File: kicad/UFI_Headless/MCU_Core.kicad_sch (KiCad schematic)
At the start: 85 parts, among them J12 FRONT, J20 GUARD, J21 LA, J4 SWD, J5 DBG_UART, SW1 RESET, SW2 BOOT, U11 APS6404L-3SQR-SN, U15 CSNP32GCR01-AOW, U5 STM32H723ZGT6, Y1 25MHz CL=12pF

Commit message: KiCad v0.7 rework, stage A9c (owner decisions of 2026-10-24): TCXO, RTC and humidity sensor on MCU_Core - X1 25 MHz TCXO HCI TC32H4-25.000-33GNDTNL (C5119013, HCMOS, +-2.5 ppm, JLC stock 1270; alternative ECS-TXO-3225-250-TR C2451321, both 1 E/D-or-NC, 2 GND, 3 OUT, 4 VDD per datasheet drawings) replaces the crystal Y1 with C38/C39: OUT drives HSE_IN (PH0), PH1 gets a no-connect, pin 1 goes to +3V3 through R132 10k, C75 100 nF at VDD, footprint Oscillator_SMD_Abracon_ASE-4Pin_3.2x2.5mm (pad order checked against both drawings); RTC: Y3 32.768 kHz Epson FC-135 Q13FC13500002 (C48615, CL 7 pF, ESR 70k; alternative Abracon ABS07 C276424) on PC14/PC15 (the two no-connects are gone) with C76/C77 10 pF C0G (C1634; CL = 5 pF + ~2 pF stray), gm_crit = 4*ESR*(2*pi*f)^2*(C0+CL)^2 = 0.76 uA/V so the LSE drive is medium-high; VBAT (pin 6) separated from +3V3 (wire and #PWR088 removed): BT1 CR2032 holder MYOUNG BS-07-A1BJ001 (C2979167, THT, KiCad footprint pad 1 = + verified against the holder drawing: + leg 12.4 mm from the cell centre) + C78 100 nF + PWR_FLAG; U25 SHT40-AD1B-R2 (C2909890, JLC stock 19423, I2C 0x44) + C79 100 nF on I2C_SCL/I2C_SDA next to the pads TP10-TP13, footprint without the die pad (Sensirion: do not solder it). Notes on the sheet for all three blocks. Four library symbols (ASE-xxxMHz, Crystal, Battery_Cell, SHT4x) were copied into the sheet cache by script because the KiCad MCP cannot inject into MCU_Core (its naive parenthesis counter trips over the STM32 pin names) - sub-unit names stay unqualified as KiCad writes them. ERC over the whole project 0 errors / 0 warnings (build/erc.rpt). Firmware in the same commit: ufi_clock.c tries RCC_HSE_BYPASS first (v1.0 TCXO) and falls back through RCC_HSE_OFF to RCC_HSE_ON after the 100 ms HSE timeout (v0.x crystal; RCC_HSE_ON alone would leave HSEBYP set), ufi_clock_hse_bypass() reports the result; new ufi_clock_rtc_init() (backup access, RTCAPB clock, backup-domain reset only for a stale non-LSE RTCSEL, LSE mediu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
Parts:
- removed C38, C39: 18pF C0G, Capacitor_SMD:C_0603_1608Metric, symbol Device:C
- removed Y1: 25MHz CL=12pF, Crystal:Crystal_SMD_3225-4Pin_3.2x2.5mm, symbol Device:Crystal_GND24
- added BT1: CR2032, Battery:BatteryHolder_MYOUNG_BS-07-A1BJ001_CR2032, symbol Device:Battery_Cell
- added C75, C78, C79: 100nF, Capacitor_SMD:C_0603_1608Metric, symbol Device:C
- added C76, C77: 10pF C0G, Capacitor_SMD:C_0603_1608Metric, symbol Device:C
- added R132: 10k, Resistor_SMD:R_0603_1608Metric, symbol Device:R
- added U25: SHT40-AD1B, Sensor_Humidity:Sensirion_DFN-4_1.5x1.5mm_P0.8mm_SHT4x_NoCentralPad, symbol Sensor_Humidity:SHT4x
- added X1: 25MHz TCXO HCMOS, Oscillator:Oscillator_SMD_Abracon_ASE-4Pin_3.2x2.5mm, symbol Oscillator:ASE-xxxMHz
- added Y3: 32.768kHz CL=7pF, Crystal:Crystal_SMD_3215-2Pin_3.2x1.5mm, symbol Device:Crystal
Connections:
- net +3V3: now also C75.1, C79.1, R132.1, U25.3 (VDD), X1.4 (Vdd); no longer U5.6 (VBAT)
- net GND: now also BT1.2 (-), C75.2, C76.2, C77.2, C78.2, C79.2, U25.4 (VSS), X1.2 (GND)
- net HSE_IN: now also X1.3 (OUT)
- net I2C_SCL: now also U25.2 (SCL)
- net I2C_SDA: now also U25.1 (SDA)
- net OSC32_IN: now reaches U5.8 (PC14)
- net OSC32_IN: now also C76.1, Y3.1
- net OSC32_OUT: now reaches U5.9 (PC15)
- net OSC32_OUT: now also C77.1, Y3.2
- net HSE_OUT: no longer names the net of U5.24 (PH1)
- new net VBAT: BT1.1 (+), C78.1, U5.6 (VBAT)
- new net X1_EN: R132.2, X1.1 (EN)
- no-connect marks 24 -> 23
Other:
- note added: "A9c (24.10.2026): X1 25 MHz TCXO (HCI TC32H4, HCMOS, +-2.5 ppm) replaces Y1/C38/C39 - OUT to OSC_IN (PH0), PH1 open, HSE runs in bypass; pin 1 E/D or NC tied to +3V3 via R132 (both HCI and the ECS alternative use 1 EN/NC, 2 GND, 3 OUT, 4 VDD). RTC: Y3 32.768 kHz Epson FC-135 (CL 7 pF, ESR 70k max) on PC14/PC15 with C76/C77 10 pF (CL = 10/2 + ~2 pF stray), gm_crit = 4*ESR*(2*pi*f)^2*(C0+CL)^2 = 0.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"
- note added: "A9c: U25 SHT40-AD1B humidity/temperature sensor (I2C 0x44, C2909890) on the I2C1 pads TP10-TP13 with C79 100 nF; pull-ups R19/R20 already on the bus. DFN-4 die pad not soldered (Sensirion recommendation). Layout (B3): at the air-inlet edge, away from U4/U19 and the drive supply path. Firmware reads it from stage A10 on."

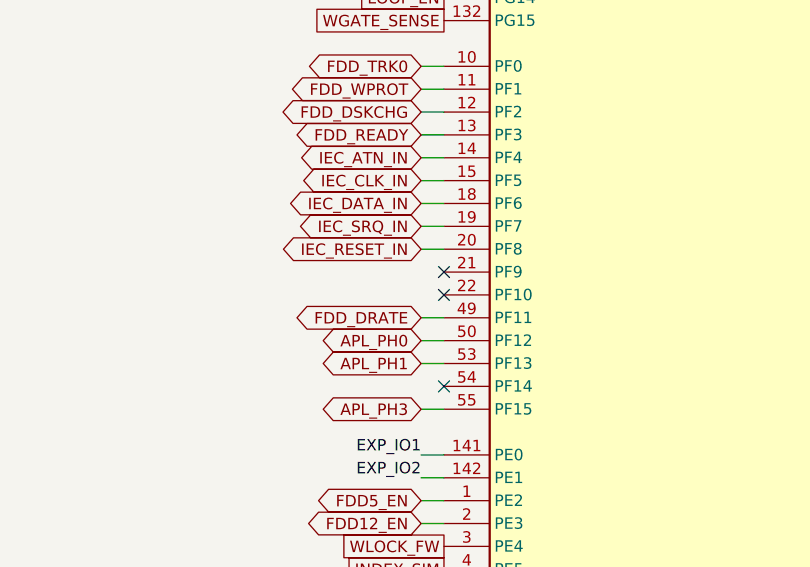
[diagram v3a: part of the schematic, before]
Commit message: KiCad v0.7 rework, stage A11c (owner's device-comparison list M2, order decided 2026-10-24: supply first): drive supplies through two TPS25921A eFuses - Power sheet: U28 (5 V) and U29 (12 V) TI TPS25921ADR (C189199, SOIC-8, JLC stock 681; new project symbol UFI_Headless:TPS25921A with the datasheet pinout 1 GND, 2 SS, 3 ENUV, 4 IN, 5 OUT, 6 FLT, 7 ILIM, 8 OVP) replace the polyfuses F2/F3 and the AO3401A/2N7002 switches Q1-Q4 with their gate network R27/R30/R32; R136/R142 150k (C22807) set the current limit to 1.43-1.7 A (datasheet table for R_ILIM = 150 k), OVP dividers R133/R134 33k/10k = 6.0 V and R138/R139/R140 100k/(10k+1k) = 14.0 V against the 1.39 V threshold (basic parts only, 91k/11k are extended), ENUV from FDD5_EN/FDD12_EN through R135/R141 10k while the existing 100k pull-downs R28/R31 keep both rails off in reset (ENUV threshold 1.39 V, 3.0 V applied), C81 2.2 nF (C1604) and C83 1 nF (C1588) give about 2.5 ms output ramp (datasheet: 1.2 nF = 3 ms at 11 V; measure at bring-up), C80/C82 100 nF at IN, FLT open drain with R137/R143 10k to +3V3 on the new global nets FLT5/FLT12; the shunts R26/R29 with U12/U13 INA180 stay behind the eFuse outputs (FDD5_F/FDD12_F -> shunt -> FDD_5V/FDD_12V, the old FDD5_S/FDD12_S nets are gone); D3 SMAJ15CA -> SMAJ13A (Diodes SMAJ13A-13-F C110519). MCU_Core: PF9 = FLT5, PF10 = FLT12 (no-connects removed). Old v0.2/v0.5 notes replaced by an A11c note. ERC over the whole project 0 errors / 0 warnings (build/erc.rpt). Firmware in the same commit: board.h/board_headless.c PIN_FLT5/PIN_FLT12 as inputs with pull-up (harmless on v0.x where the pins are open), ufi_board.c sample_faults() reads FLT only on board_rev >= 10 and only for a rail that is switched on (FLT is also low while ENUV is low), reports a change once as POWER event 0x83 with ERR LED and leaves the rail on because the eFuse retries by itself, board_status.power bits 2/3 carry the fault state; overcurrent comment updated (eFuse limit instead of polyfuse hold). Protocol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
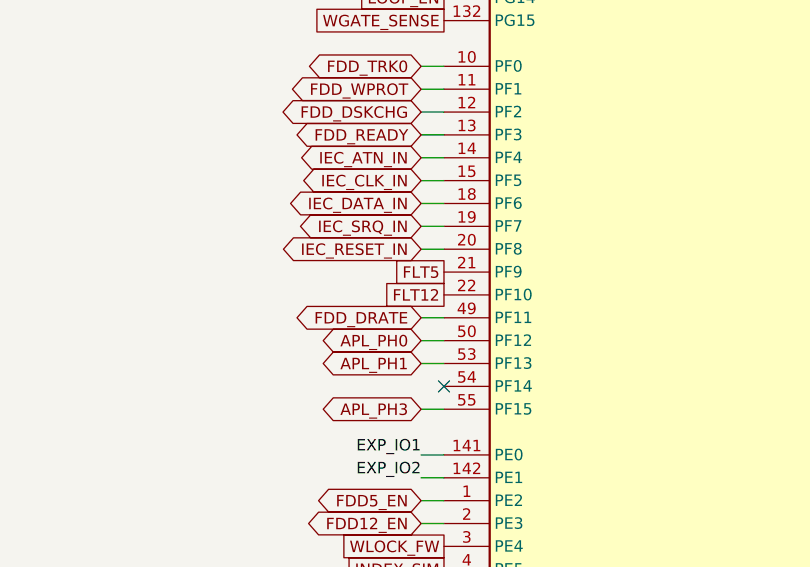
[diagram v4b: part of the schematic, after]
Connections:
- net FLT5: now reaches U5.21 (PF9)
- net FLT12: now reaches U5.22 (PF10)
- no-connect marks 23 -> 21

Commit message: KiCad v0.7 rework, stage A11d part 1 (owner's device-comparison list M5, S1-S4, S6; pins per docs/Timer_Zuteilung.md): sync sensor, J6 pin 2/4/33, rail voltage sense - Apple_Port: J19 pin 3 leaves the INDEX bus and becomes SYNC_5V with R165 10k to +3V3 and D30 PESD3V3L1BA, the new third Schmitt inverter U26 74LVC14AD (C133541, single-unit project symbol UFI_Headless:74LVC14_1U) turns it into SYNC -> PC6 (TIM8_CH1, AF3), also reads J6 pin 2 (FD_DENSITY) and pin 4 (FD_PIN4) back as FDD_PIN2_IN -> PD14 / FDD_PIN4_IN -> PD15 and reserves input 9 for the Mac !CSTOUT line of K1 (no-connect until A11d part 2), unused inputs on GND, C86 100 nF. FDD_Connectors: J6 pin 4 gets its own open-drain output Q12 BSS138DW (C154900, channel 1, gate FDD_PIN4 = PF14 with R158 100k, termination R159 1k to FDD_5V); J6 pin 33 moves from a fixed GND to the solder jumper JP7 (bridged to GND by default) whose third pad carries FLIPPY = PB5 through R156 2.2k with R157 2.2k to GND (2.2k instead of the planned 2.4k because 2.2k C4190 is already in the BOM). Power: R160/R161 10k/10k (FDD_5V / 2 -> V_FDD5 = PC4, ADC1 INP4) and R162/R163 33k/10k (FDD_12V / 4.3 -> V_FDD12 = PC5, ADC1 INP8). MCU_Core: no-connects on PC6, PD14, PD15, PF14, PB5, PC4, PC5, PB1 replaced by the global labels; PB0 (MAC_SEL) and PA8 (MAC_PWM) stay no-connect until the Mac header comes in part 2, PB1 = MAC_CSTOUT is already wired to U26. ERC over the whole project 0 errors / 0 warnings (build/erc.rpt). Firmware in the same commit: board.h/board_headless.c define PIN_SYNC, PIN_FDD_PIN2_IN, PIN_FDD_PIN4_IN, PIN_FDD_PIN4, PIN_FDD_PIN33, PIN_MAC_SEL, PIN_MAC_PWM, PIN_MAC_CSTOUT and ADC_CH_V_FDD5/V_FDD12 and initialise them as inputs or released (low) outputs; the TIM8 capture of SYNC, the rail-voltage limits (4.5 V / 10.8 V) and the protocol access follow in stage A10 (protocol doc: one hunk in the INDEX_SIM bullet - the sync sensor no longer drives the INDEX bus on v1.0, apple_sync has no effect there until A10). ARM build 0 wa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
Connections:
- net FDD_PIN33: now reaches U5.135 (PB5)
- net V_FDD5: now reaches U5.44 (PC4)
- net V_FDD12: now reaches U5.45 (PC5)
- net MAC_CSTOUT: now reaches U5.47 (PB1)
- net FDD_PIN4: now reaches U5.54 (PF14)
- net FDD_PIN2_IN: now reaches U5.85 (PD14)
- net FDD_PIN4_IN: now reaches U5.86 (PD15)
- net SYNC: now reaches U5.96 (PC6)
- no-connect marks 21 -> 13

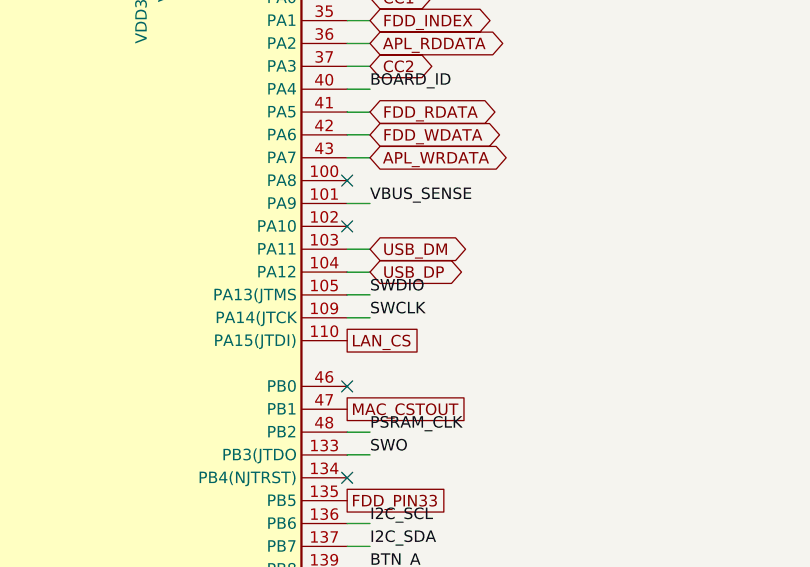
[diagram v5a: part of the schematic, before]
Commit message: KiCad v0.7 rework, stage A11d part 2 (owner's list S5, S7, K1; owner decisions 2026-10-24: no D-sub on the board, pins 9/20 through solder jumpers default open, PWM line always on a Schmitt input, no fuse on the -12 V): Apple_Port: new Mac 3.5" port J23 (2x10 IDC, UFI_Headless:IDC-Header_2x10_P2.54mm_Vertical_UFI, C2977593) in the Apple internal 20-pin floppy pinout taken from the tashnotes connector document - 1/3/5/7 GND, 2/4/6/8 CA0/CA1/CA2/LSTRB on the Disk II phase nets AP_PH0-3, 10 !WRREQ (AP_WRREQ, gated by LOCK since A11a), 12 SEL = MAC_SEL_5V, 14 !ENBL = AP_EN2 (J15 removed), 16 RD = AP_RDDATA, 18 WR = AP_WRDATA, 11 FDD_5V, 13/15/17/19 FDD_12V, 9 = AP_M12V_J6 only through JP6 (open; 800K/FDHD drives output !EJECT there), 20 = CSTOUT_5V with R166 10k to FDD_5V, fed by the PWM driver only through JP5 (open; 800K/FDHD output !CSTOUT there) and always read back through U26 pin 9 -> MAC_CSTOUT = PB1; U27 SN74AHCT244PWR (C484743, FDD_5V, C87 100 nF) shifts MAC_SEL (PB0) and MAC_PWM (PA8, TIM1_CH1) to 5 V, unused inputs on GND and unused outputs no-connect; D31 ESDA6V1-5SC6 (C6650) on SEL and pin 20. S5: JP8 (bridged) between the ICL7662 output AP_M12V and J14 pin 9 (AP_M12V_J), no fuse - the pump limits to about 20 mA; U18 stays the ICL7662. Power: S7 USB shield J1 SH leaves GND and goes through R164 1M (C22935) parallel C85 4.7 nF (C53987) to GND (net USB_SHIELD). MCU_Core: PB0 = MAC_SEL and PA8 = MAC_PWM wired (no-connects removed). Notes on the Apple sheet. ERC over the whole project 0 errors / 0 warnings (build/erc.rpt). No firmware change in this part (the pins were defined and initialised released in part 1; the Mac drive driver SEL/PWM/CSTOUT and the 800K/FDHD GCR path are a firmware stage after A10), therefore no protocol change. PLAN.md (A11d complete, A11 done except the layout), kicad README (A11d-2 row). PCB follows in B3 (J23 placement with cable exit towards the enclosure socket).
Claude-Session: https://claude.ai/code/session_014MdzrcyXuayppPHbfEjU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
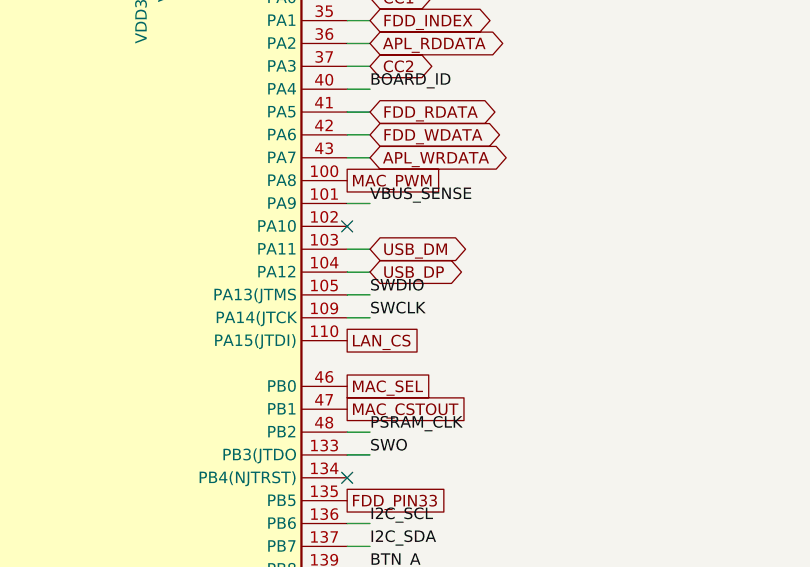
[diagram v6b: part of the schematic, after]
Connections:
- net MAC_PWM: now reaches U5.100 (PA8)
- net MAC_SEL: now reaches U5.46 (PB0)
- no-connect marks 13 -> 11

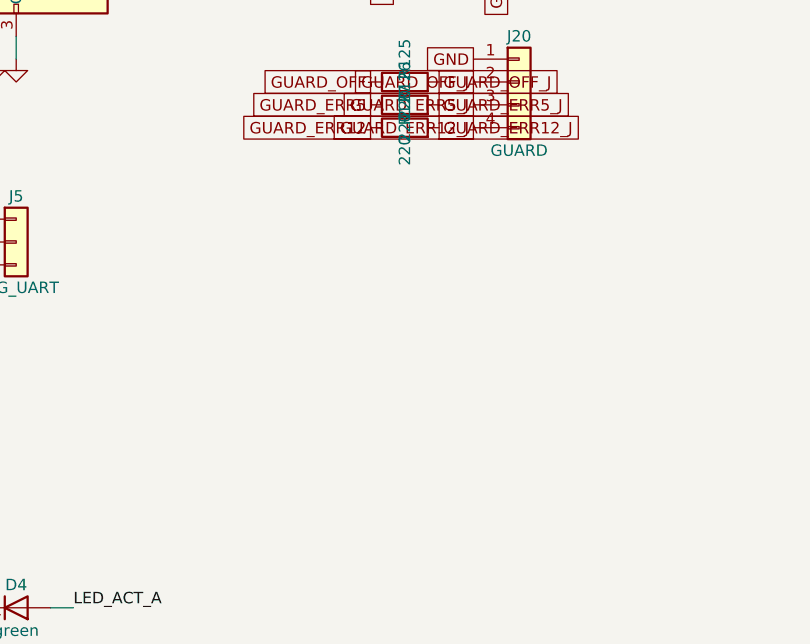
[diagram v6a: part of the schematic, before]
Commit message: KiCad v0.7 rework, stage A11f (fixes from the A8 review, owner decisions of 2026-10-25): F1 - the write gate is now hard-gated by a NOR instead of the A11a OR that had driven the MOSFET gate the wrong way since A11b: new U31 74LVC1G02 (MDD 74LVC1G02GW C52953351, SOT-353) on Flux_Interface forms Q9 gate = NOR(WGATE_n, LOCK), PE14 becomes WGATE_n (active low on every board revision again) with R167 10k pull-up to +3V3 so reset and boot leave the gate released, C88 100 nF; U30 gate 1 retired (1A/1B on GND, 1Y no-connect), gate 2 still gates APL_WRREQ with LOCK; netlist: FDD_WGATE = U5.67 R167 U31.1 J21.7, FDD_WGATE_G = U31.4 Q9.2 R151 TP8, LOCK = U14.4 U30.6 U31.2. Firmware in the same commit: board.h bus_out_inverted() excludes PE14, board_headless.c latches PE14 high at start-up; truth table for every MOSFET-driven line (reset / idle / active) recorded in PLAN.md, measurement point "J6 pin 24 stays high with the lock set during a read" in the README row, self-test item planned for A10; protocol doc (one hunk in the board_status bit 0 note). R1: D30 removed, SYNC_5V protected by the 5 V channel IO3 of D31 ESDA6V1-5SC6, J19 becomes a keyed JST B3B-XH-A (C144394). R2: J20 GUARD becomes JST B4B-XH-A (C144395) with D32-D34 PESD3V3L1BA (C51450) on GUARD_OFF_J/ERR5_J/ERR12_J; note that the Guard board v0.2 gets a JST XH J3 too. R3: flippy divider kept at 2.4k/2.4k (C22940, Greaseweazle V4.1 compatible), JP7 default GND. ERC over the whole project 0 errors / 0 warnings (build/erc.rpt). ARM build 0 warnings; offline gate as reported in the stage log. PLAN.md (A11f, polarity table), kicad README (A11f row). PCB follows in B3.
Claude-Session: https://claude.ai/code/session_014MdzrcyXuayppPHbfEjUrw
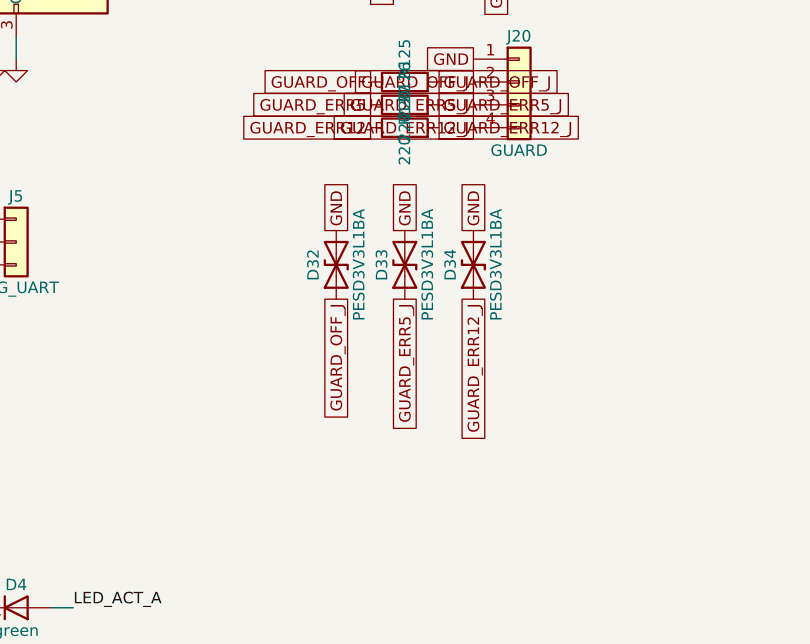
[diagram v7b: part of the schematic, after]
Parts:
- added D32, D33, D34: PESD3V3L1BA, Diode_SMD:D_SOD-323, symbol Device:D_TVS
- J20: footprint Connector_PinHeader_2.54mm:PinHeader_1x04_P2.54mm_Vertical -> Connector_JST:JST_XH_B4B-XH-A_1x04_P2.50mm_Vertical; LCSC (none) -> C144395; MPN (none) -> JST B4B-XH-A (GUARD, keyed; A11f R2 - Guard board v0.2: its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
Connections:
- net GND: now also D32.2 (A2), D33.2 (A2), D34.2 (A2)
- net GUARD_ERR12_J: now also D34.1 (A1)
- net GUARD_ERR5_J: now also D33.1 (A1)
- net GUARD_OFF_J: now also D32.1 (A1)

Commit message: KiCad v0.7 rework, stage C part 1 (BOM completion before the release, review note H12): every BOM row now carries an LCSC number, checked against the JLCPCB SMT catalogue on 2026-10-25 (stock in brackets). LAN sheet: U23 W5500 C32843 (9019), J22 HR911105A C12074 (72229, THT), Y2 25 MHz 12 pF +-10 ppm YXC X322525MOB4SI C9006 (basic; load capacitance 12 pF verified on the LCSC parameter page, fits the 18 pF C59/C60), C59/C60 18 pF C0G Yageo CC0603JRNPO9BN180 C107040, C61/C74 10 nF FH 0603B103K500NT C57112 (basic), C71 22 nF Samsung CL10B223KB8NNNC C21122 (basic), C72/C73 6.8 nF FH 0603B682K500NT C1631 (basic), C62 4.7 uF C1779, C63/C69 10 uF C15850, C64-C68/C70 100 nF C14663, FB2 C1002, R109 1M C22935, R111 12.4k 1 % C22865, R112/R113 49.9R 1 % C23185 (basic), R114 10R 1 % C22859 (basic), R115/R116 82R 1 % C23255, R117/R118 330R C23138, R119-R124 10k C25804. Other sheets: R75-R99/R105/R128 1k C21190, R74/R107/R108 10k C25804, R101-R104/R130 470R C23179, R106/R131 100k C25803, C58 100 nF C14663 (value text 100n -> 100nF so it groups with the other 100 nF), D18-D26/D28/D29 PESD3V3L1BA C51450 (48710) like D32-D34, Q5 2N7002 C8545 (basic), U22 TS5A3166DBVR C353035 (10678), J2 DC-005 2.0 C16214 (92305; same pin pattern as the KiCad BarrelJack_Horizontal footprint, placement to be checked in the JLC viewer), J7 2x12 IDC ZHOURI DC3-2.54-24PAS C5144580 (stock 81 - hand soldering stays the recommendation in docs/Bestellung_JLC.md), J12 2x8 IDC DC3-2.54-16PAS C2977594 (4335), J16 2x5 pin header XFCN PZ254V-12-10P C492422 (105667), J21 2x10 pin header PZ254V-12-20P C492427 (63622). Solder jumpers JP5-JP8 are excluded from the BOM (in_bom no) like JP1/JP3 - bare copper, nothing to place. Stock of the review's watch list: U9 SN74LS07DR C371970 4776, D31 ESDA6V1-5SC6 C6650 3010, L1 SRN6045TA-150M C1330797 1866. BOM export (kicad-cli sch export bom, grouped by value/footprint/LCSC): 99 rows, 0 without LCSC, 0 DNP. ERC over the whole project 0 errors / 0 warnings (build/erc.rpt). No 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
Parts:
- D18, D19, D20, D21, D22, D23, D24, D25, D26, D28, D29: LCSC (none) -> C51450
- J12: LCSC (none) -> C2977594
- J21: LCSC (none) -> C492427
- R101, R102, R103, R104, R130: LCSC (none) -> C23179
- R105, R128: LCSC (none) -> C21190
- R107, R108: LCSC (none) -> C25804
